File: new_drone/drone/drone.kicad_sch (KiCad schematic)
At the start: 61 parts, among them J1 Conn_01x06, J2 XT60-M, SW1 SW_Push_Open, SW2 SW_Push_Open, U1 ESP32-WROOM-32, U2 MPU-6050, U3 MCP8063, U4 BMP280, U5 MCP8063, U6 MCP8063, U7 MCP8063, U9 LM1117MP-3.3

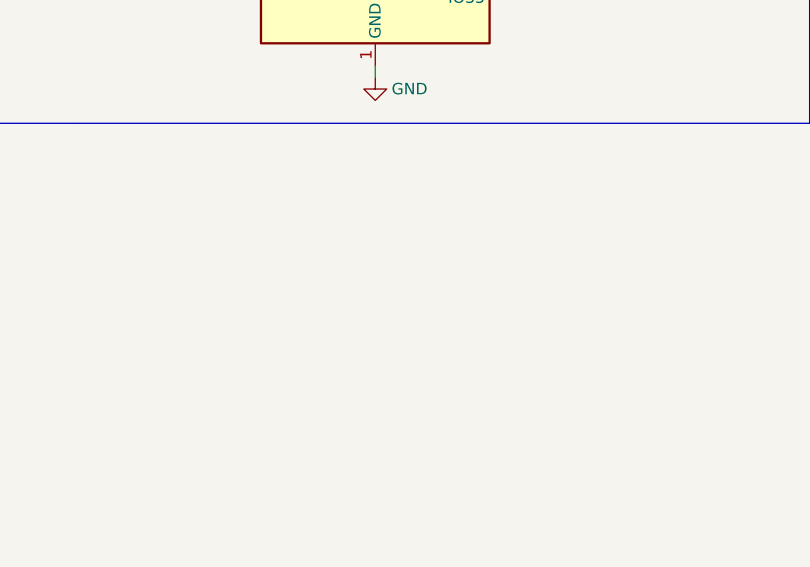
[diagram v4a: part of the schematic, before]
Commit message: add openmv cam pin
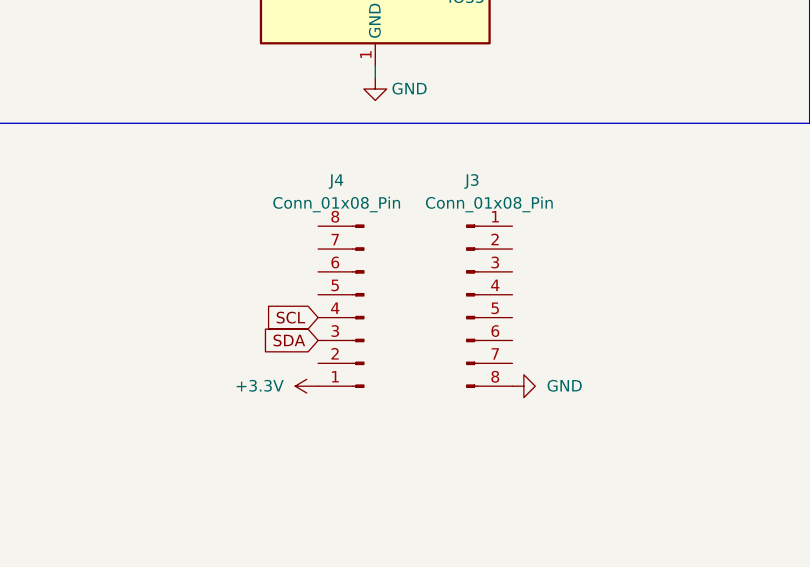
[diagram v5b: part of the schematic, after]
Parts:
- added J3, J4: Conn_01x08_Pin, Connector_PinSocket_2.54mm:PinSocket_1x08_P2.54mm_Vertical, symbol Connector:Conn_01x08_Pin
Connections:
- net +3.3V: now also J4.1 (Pin_1)
- net GND: now also J3.8 (Pin_8)
- net SCL: now also J4.4 (Pin_4)
- net SDA: now also J4.3 (Pin_3)
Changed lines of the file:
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@@
+    )
+  )
+  (global_label "SDA" (shape input) (at 149.86 123.19 180) (fields_autoplaced)
+    (effects (font (size 1.27 1.27)) (justify right))
+    (property "Intersheetrefs" "${INTERSHEET_REFS}" (at 143.3067 123.19 0)
+      (effects (font (size 1.27 1.27)) (justify right) hide)
     )
   )
@@
     (effects (font (size 1.27 1.27)) (justify right))
     (property "Intersheetrefs" "${INTERSHEET_REFS}" (at 13.1293 34.2106 0)
+      (effects (font (size 1.27 1.27)) (justify right) hide)
+    )
+  )
+  (global_label "SCL" (shape input) (at 149.86 120.65 180) (fields_autoplaced)
+    (effects (font (size 1.27 1.27)) (justify right))
+    (property "Intersheetrefs" "${INTERSHEET_REFS}" (at 143.3672 120.65 0)
       (effects (font (size 1.27 1.27)) (justify right) hide)
     )
@@
     )
   )
+  (symbol (lib_id "power:GND") (at 171.45 128.27 90) (unit 1)
+    (in_bom yes) (on_board yes) (dnp no) (fields_autoplaced)
+    (property "Reference" "#PWR033" (at 177.8 128.27 0)
+      (effects (font (size 1.27 1.27)) hide)
+    )
+    (property "Value" "GND" (at 175.26 128.27 90)
+      (effects (font (size 1.27 1.27)) (justify right))
+    )
+    (property "Footprint" "" (at 171.45 128.27 0)
+      (effects (font (size 1.27 1.27)) hide)
+    )
+    (property "Datasheet" "" (at 171.45 128.27 0)
+      (effects (font (size 1.27 1.27)) hide)
+    )
+    (pin "1")
+    (instances
+      (project "drone"
+        (path "/9041473b-952f-40b0-8946-ac9ea300810a"
+          (reference "#PWR033") (unit 1)
+        )
+      )
+    )
+  )
   (symbol (lib_id "Regulator_Linear:LM1117MP-3.3") (at 53.34 163.83 0) (unit 1)
     (in_bom yes) (on_board yes) (dnp no) (fields_autoplaced)
@@
     )
   )
+  (symbol (lib_id "power:+3.3V") (at 149.86 128.27 90) (unit 1)
+    (in_bom yes) (on_board yes) (dnp no) (fields_autoplaced)
+    (property "Reference" "#PWR034" (at 153.67 128.27 0)
+      (effects (font (size 1.27 1.27)) hide)
+    )
+    (property "Value" "+3.3V" (at 146.05 128.27 90)
+      (effects (font (size 1.27 1.27)) (justify left))
+    )
+    (property "Footprint" "" (at 149.86 128.27 0)
+      (effects (font (size 1.27 1.27)) hide)
+    )
+    (property "Datasheet" "" (at 149.86 128.27 0)
+      (effects (font (size 1.27 1.27)) hide)
+    )
+    (pin "1")
+    (instances
+      (project "drone"
+        (path "/9041473b-952f-40b0-8946-ac9ea300810a"
+          (reference "#PWR034") (unit 1)
+        )
+      )
+    )
+  )
   (symbol (lib_id "Device:R_Small") (at 179.07 22.86 0) (unit 1)
     (in_bom yes) (on_board yes) (dnp no) (fields_autoplaced)
@@
     )
   )
+  (symbol (lib_id "Connector:Conn_01x08_Pin") (at 154.94 120.65 180) (unit 1)
+    (in_bom yes) (on_board yes) (dnp no)
+    (property "Reference" "J4" (at 151.13 105.41 0)
+      (effects (font (size 1.27 1.27)) (justify right))
+    )
+    (property "Value" "Conn_01x08_Pin" (at 144.78 107.95 0)
+      (effects (font (size 1.27 1.27)) (justify right))
+    )
+    (property "Footprint" "Connector_PinSocket_2.54mm:PinSocket_1x08_P2.54mm_Vertical" (at 154.94 120.65 0)
+      (effects (font (size 1.27 1.27)) hide)
+    )
+    (property "Datasheet" "~" (at 154.94 120.65 0)
+      (effects (font (size 1.27 1.27)) hide)
+    )
+    (pin "1")
+    (pin "2")
+    (pin "3")
+    (pin "4")
+    (pin "5")
+    (pin "6")
+    (pin "7")
+    (pin "8")
+    (instances
+      (project "drone"
+        (path "/9041473b-952f-40b0-8946-ac9ea300810a"
+          (reference "J4") (unit 1)
+        )
+      )
+    )
+  )
   (symbol (lib_name "MCP8063_1") (lib_id "MCP8063:MCP8063") (at 245.11 138.43 0) (unit 1)
     (in_bom yes) (on_board yes) (dnp no) (fields_autoplaced)
@@
         )
       )
+    )
+  )
+  (symbol (lib_id "Connector:Conn_01x08_Pin") (at 166.37 118.11 0) (unit 1)
+    (in_bom yes) (on_board yes) (dnp no)
+    (property "Reference" "J3" (at 167.005 105.41 0)
+      (effects (font (size 1.27 1.27)))
+    )
+    (property "Value" "Conn_01x08_Pin" (at 168.91 107.95 0)
+      (effects (font (size 1.27 1.27)))
+    )
+    (property "Footprint" "Connector_PinSocket_2.54mm:PinSocket_1x08_P2.54mm_Vertical" (at 166.37 118.11 0)
+      (effects (font (size 1.27 1.27)) hide)
+    )
+    (property "Datasheet" "~" (at 166.37 118.11 0)
+      (effects (font (size 1.27 1.27)) hide)
+    )
+    (pin "1")
+    (pin "2")
+    (pin "3")
+    (pin "4")
+    (pin "5")
+    (pin "6")
+    (pin "7")
+    (pin "8")
+    (instances
+      (project "drone"
+        (path "/9041473b-952f-40b0-8946-ac9ea300810a"
+          (reference "J3") (unit 1)
+        )
+      )

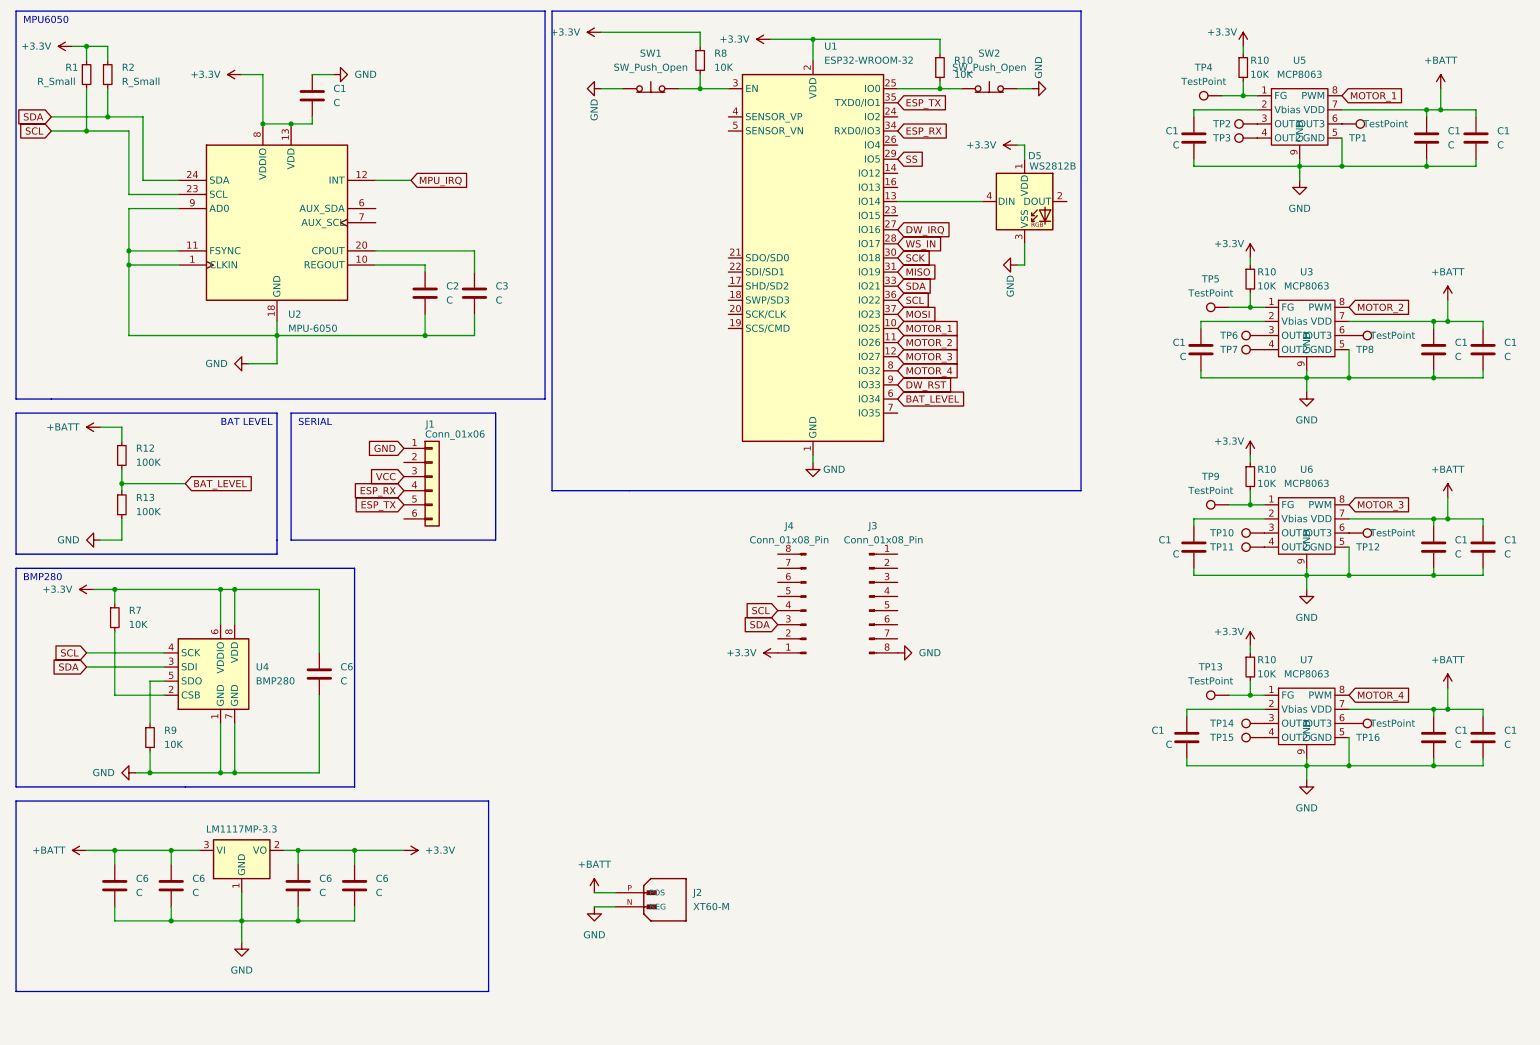
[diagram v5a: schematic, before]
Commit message: mpu6050 to 9250
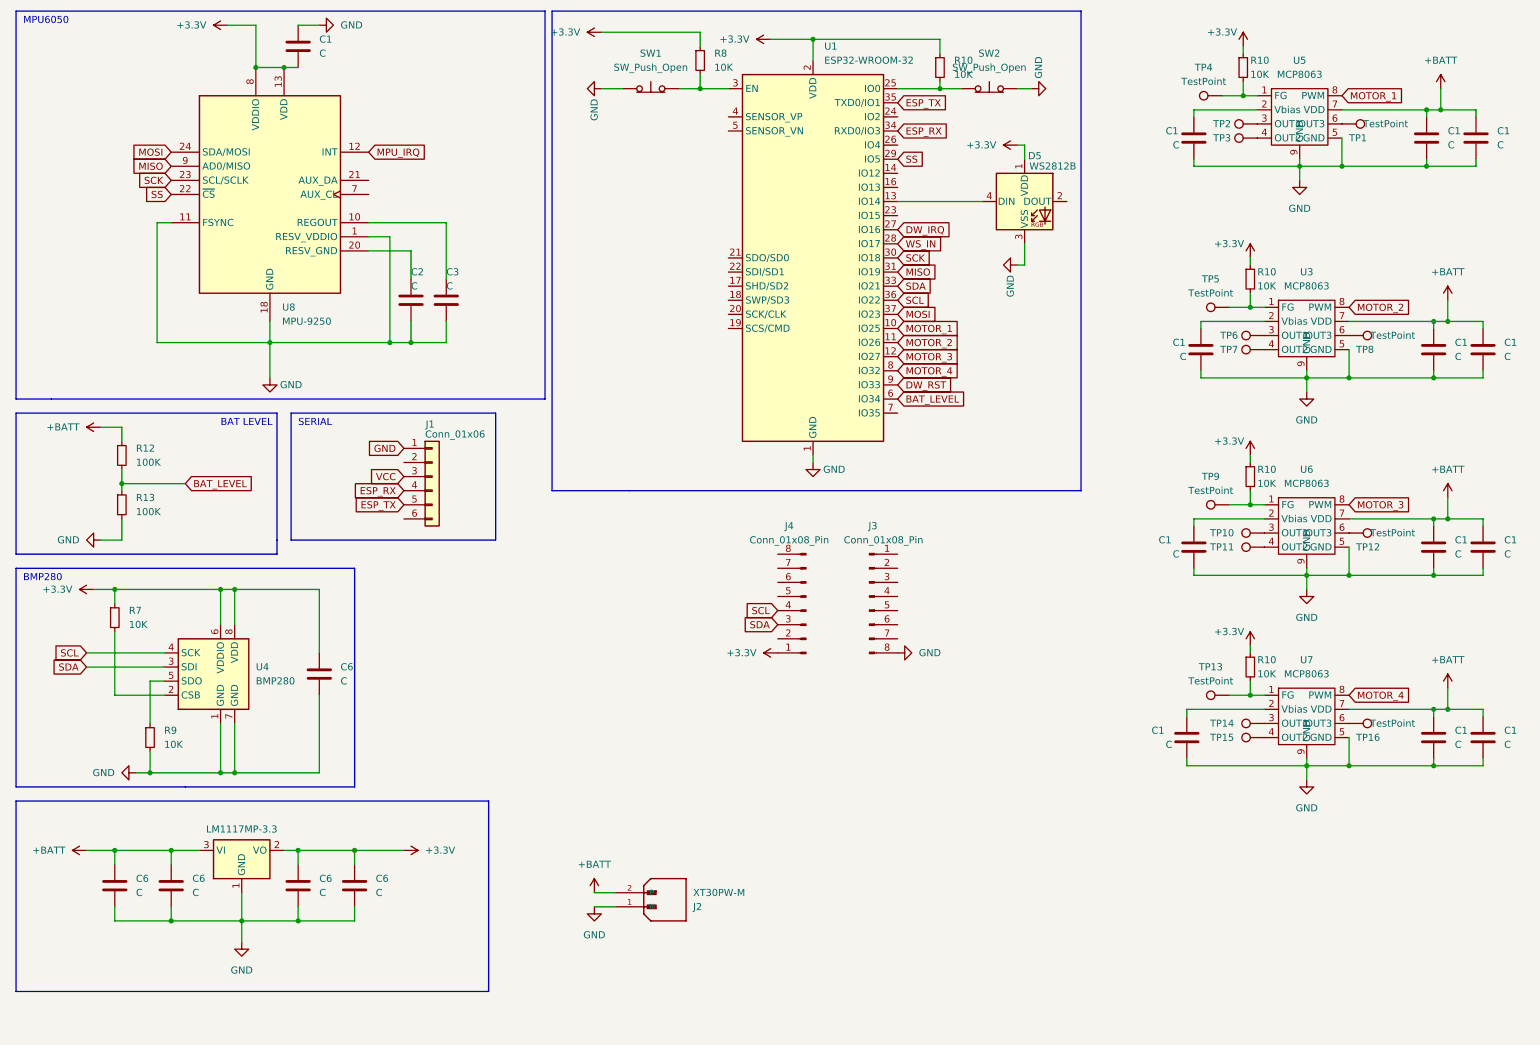
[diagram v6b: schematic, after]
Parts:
- removed J2: XT60-M, Connector_AMASS:AMASS_XT60-M_1x02_P7.20mm_Vertical, symbol XT60:XT60-M
- removed R1, R2: R_Small, Resistor_SMD:R_0603_1608Metric, symbol Device:R_Small
- removed U2: MPU-6050, Sensor_Motion:InvenSense_QFN-24_4x4mm_P0.5mm, symbol Sensor_Motion:MPU-6050
- added J2: XT30PW-M, Connector_AMASS:AMASS_XT30U-F_1x02_P5.0mm_Vertical, symbol XT30:XT30PW-M
- added U8: MPU-9250, Sensor_Motion:InvenSense_QFN-24_3x3mm_P0.4mm, symbol Sensor_Motion:MPU-9250
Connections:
- net +3.3V: now also U8.13 (VDD), U8.8 (VDDIO)
- net +BATT: now also J2.2 (P)
- net GND: now also J2.1 (N), U8.1 (RESV_VDDIO), U8.11 (FSYNC), U8.18 (GND)
- net MISO: now also U8.9 (AD0/MISO)
- net MOSI: now also U8.24 (SDA/MOSI)
- net MPU_IRQ: now also U8.12 (INT)
- net SCK: now also U8.23 (SCL/SCLK)
- net SS: now also U8.22 (~{CS})
- net at C2.1: now also U8.20 (RESV_GND)
- net at C3.1: now also U8.10 (REGOUT)
